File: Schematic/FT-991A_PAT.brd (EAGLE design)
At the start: 44.6 x 59.8 mm, 30 parts, among them Q1 PE4259, Q2 MC78L09ABDR2GOSCT, Q5 NCP553, Q7 J310, Q8 5086, X1 IF_IN, X2 SCP_OUT, X3 SDR_OUT

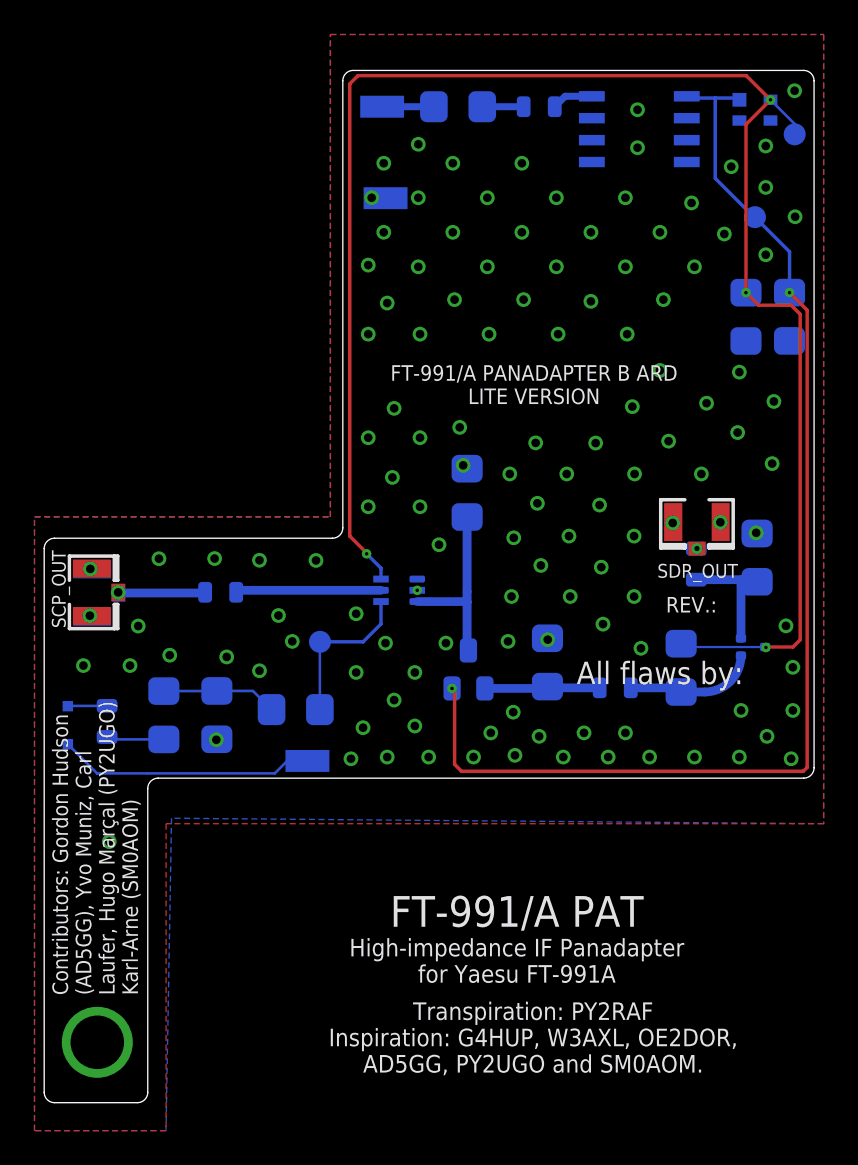
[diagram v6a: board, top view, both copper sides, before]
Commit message: Christening Rev. R
* New PDF files
* Voltage regulator re-routing
* Larger NCP533 and Diode pads
* Fixed some BOM errors
* Removed some old files
* Added Eagle Library file
* Fixed Readme links
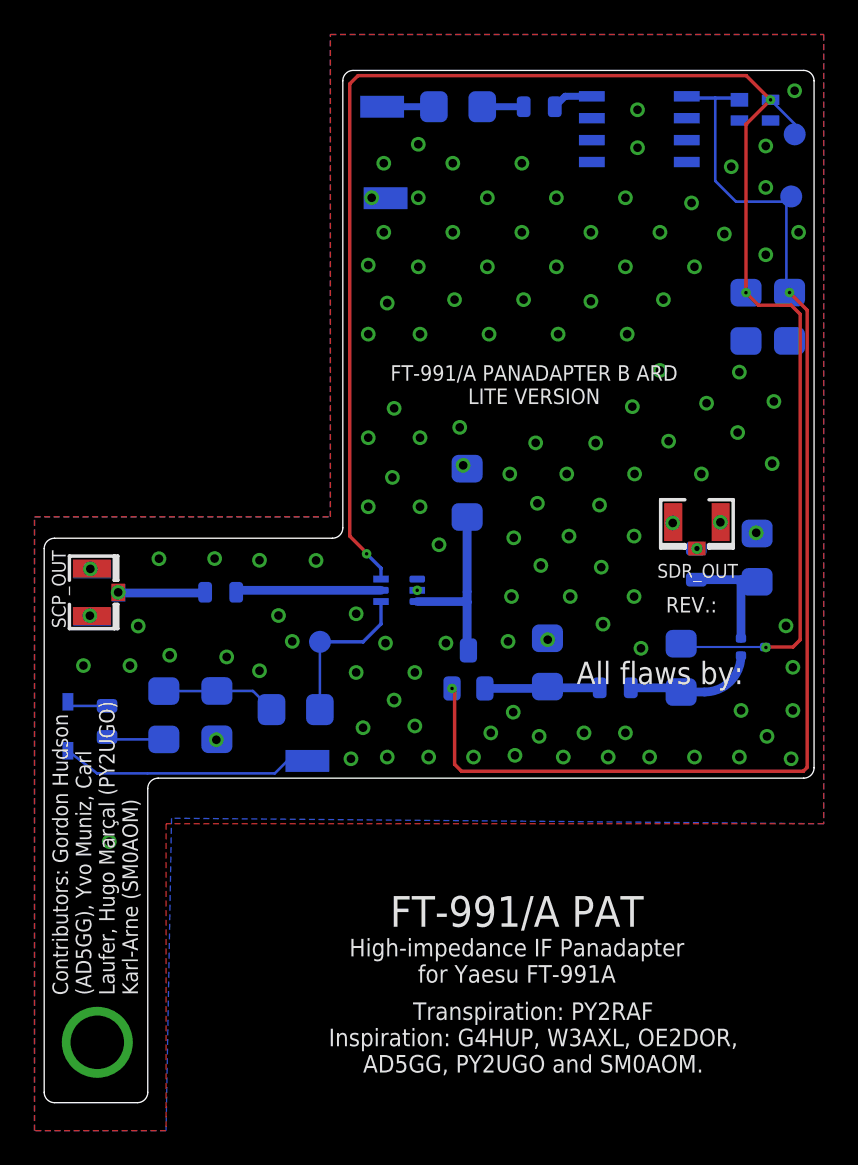
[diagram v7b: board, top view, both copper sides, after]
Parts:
- moved TP1 2.42 mm to (49.6, 64.1)
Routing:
- net 9V: track 69.3 -> 72.1 mm
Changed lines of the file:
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@@
 <text x="14.7" y="39.8" size="1.3" layer="29" font="vector" ratio="15" rot="R180" align="center">Light
 Ed</text>
-<text x="50.6" y="66" size="0.8" layer="22" font="vector" ratio="15" rot="MR0">3V</text>
-<text x="46.5" y="62.9" size="0.8" layer="22" font="vector" ratio="15" rot="MR0">9V</text>
+<text x="50.3" y="65.7" size="0.8" layer="22" font="vector" ratio="15" rot="MR0">3V</text>
+<text x="48.7" y="62.9" size="0.8" layer="22" font="vector" ratio="15" rot="MR0">9V</text>
 <text x="24.6" y="38" size="0.8" layer="22" font="vector" ratio="15" rot="MR0">sw</text>
 <text x="42" y="34.9" size="1.3" layer="29" font="vector" ratio="15" rot="R180" align="center">PY2RAF</text>
@@
 </element>
 <element name="Q1" library="aarf" package="SC-70" value="PE4259" x="26.9" y="41.3" smashed="yes" rot="MR270"/>
-<element name="TP1" library="testpad" library_urn="urn:adsk.eagle:library:385" package="B1,27" package3d_urn="urn:adsk.eagle:package:27944/1" value="9V" x="47.5" y="62.9" smashed="yes" rot="MR0">
-<attribute name="TP_SIGNAL_NAME" value="" x="48.135" y="60.995" size="1" layer="38" rot="MR0"/>
-<attribute name="VALUE" x="48.135" y="62.138" size="0.0254" layer="28" rot="MR0"/>
+<element name="TP1" library="testpad" library_urn="urn:adsk.eagle:library:385" package="B1,27" package3d_urn="urn:adsk.eagle:package:27944/1" value="9V" x="49.6" y="64.1" smashed="yes" rot="MR0">
+<attribute name="TP_SIGNAL_NAME" value="" x="50.235" y="62.195" size="1" layer="38" rot="MR0"/>
+<attribute name="VALUE" x="50.235" y="63.338" size="0.0254" layer="28" rot="MR0"/>
 </element>
 <element name="TP2" library="testpad" library_urn="urn:adsk.eagle:library:385" package="B1,27" package3d_urn="urn:adsk.eagle:package:27944/1" value="3V" x="49.8" y="67.7" smashed="yes" rot="MR0">
@@
 <via x="8.995" y="42.525" extent="1-16" drill="0.5"/>
 <via x="40.525" y="48.025" extent="1-16" drill="0.5"/>
-<via x="49.825" y="62.925" extent="1-16" drill="0.5"/>
+<via x="50.025" y="62.025" extent="1-16" drill="0.5"/>
 <via x="30.095" y="58.125" extent="1-16" drill="0.5"/>
 <via x="32.095" y="56.125" extent="1-16" drill="0.5"/>
@@
 <wire x1="19.6775" y1="30.6775" x2="12.311253125" y2="30.6775" width="0.15" layer="16"/>
 <wire x1="12.311253125" y1="30.6775" x2="9.388746875" y2="30.6775" width="0.1524" layer="16"/>
-<wire x1="9.388746875" y1="30.6775" x2="7.69535625" y2="32.370890625" width="0.1524" layer="16"/>
+<wire x1="9.388746875" y1="30.6775" x2="7.69535625" y2="31.989890625" width="0.1524" layer="16"/>
 </signal>
 <signal name="N$35">
@@
 <contactref element="L3" pad="P$1"/>
 <wire x1="9.9662" y1="34.58748125" x2="7.711946875" y2="34.58748125" width="0.1524" layer="16"/>
-<wire x1="7.711946875" y1="34.58748125" x2="7.69535625" y2="34.570890625" width="0.1524" layer="16"/>
+<wire x1="7.711946875" y1="34.58748125" x2="7.69535625" y2="34.824890625" width="0.1524" layer="16"/>
 </signal>
 <signal name="FINAL">
@@
 <wire x1="43.655" y1="69.8" x2="43.55" y2="69.905" width="0.2" layer="16"/>
 <wire x1="46.5" y1="69.8" x2="46.6" y2="69.7" width="0.2" layer="16"/>
-<wire x1="47.5" y1="62.9" x2="47.45" y2="62.9" width="0.2" layer="16"/>
-<wire x1="47.45" y1="62.9" x2="45.2" y2="65.15" width="0.2" layer="16"/>
-<wire x1="45.2" y1="69.8" x2="45.2" y2="65.15" width="0.2" layer="16"/>
-<wire x1="47.5" y1="62.9" x2="49.5025" y2="60.8975" width="0.2" layer="16"/>
-<wire x1="49.5025" y1="60.8975" x2="49.5025" y2="58.5325" width="0.2" layer="16"/>
+<wire x1="49.6" y1="58.63" x2="49.5025" y2="58.5325" width="0.1524" layer="16"/>
+<wire x1="49.4" y1="64.1" x2="49.6" y2="64.1" width="0.1524" layer="16"/>
+<wire x1="49.3178" y1="63.8178" x2="49.3178" y2="58.7172" width="0.1524" layer="16"/>
+<wire x1="49.5025" y1="58.5325" x2="49.3178" y2="58.7172" width="0.1524" layer="16"/>
+<wire x1="49.3178" y1="63.8178" x2="49.6" y2="64.1" width="0.1524" layer="16"/>
+<wire x1="49.6" y1="64.1" x2="49.3" y2="63.8" width="0.1524" layer="16"/>
+<wire x1="46.4" y1="63.8" x2="45.2" y2="65" width="0.1524" layer="16"/>
+<wire x1="49.3" y1="63.8" x2="46.4" y2="63.8" width="0.1524" layer="16"/>
+<wire x1="45.2" y1="65" x2="45.2" y2="69.8" width="0.1524" layer="16"/>
 </signal>
 <signal name="3V">

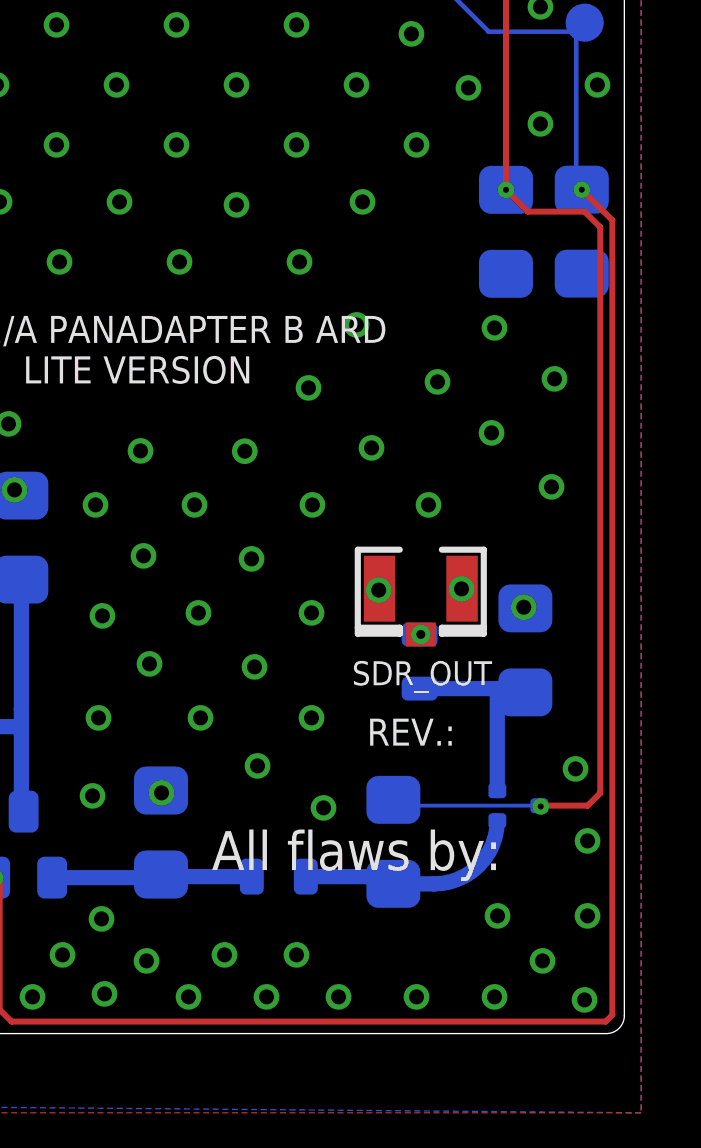
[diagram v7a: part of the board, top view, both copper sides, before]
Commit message: Announcing: Rev. S
* Replaced 2SC5086 with BFR193F amplifier, since 2SC5086 is now EOL
* Added a RF choke (L1) to avoid signal feedback propagating in 3V line
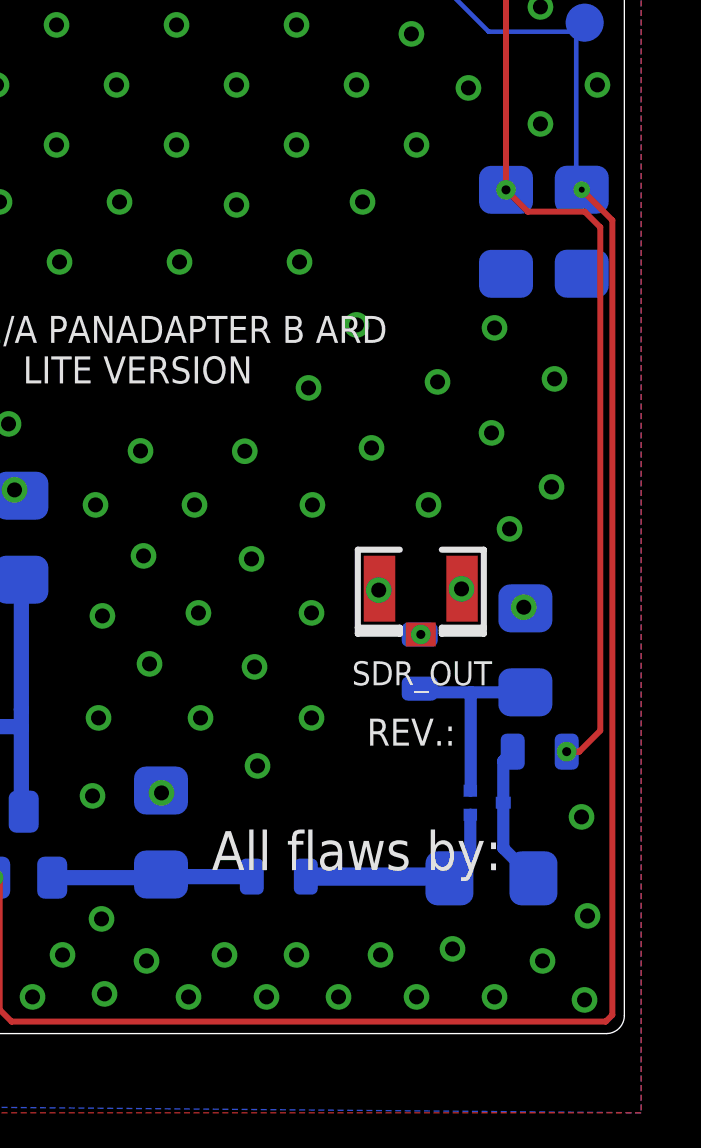
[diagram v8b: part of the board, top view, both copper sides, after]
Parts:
- added L1: 3.9uH, aarf:0805
- Q8: value 5086 -> BFR193F; device aarf:2-2H1A -> aarf:TSFP-3
- moved R8 3.49 mm to (46.5, 35.6), turned to 0 degrees
- moved Q8 1.00 mm to (46.4, 38.1)
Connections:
- new net FB-3V: L1.P$2, Q8.3, R8.1
- net 3V: now also L1.P$1; no longer Q8.3, R8.1
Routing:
- net 3V: track 98.5 -> 90.6 mm
- net FB-3V: track 0.00 -> 4.78 mm
